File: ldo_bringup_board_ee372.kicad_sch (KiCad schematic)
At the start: 69 parts, among them J1 VIN, J10 MD_SW_EN, J2 GND, J3 IBIAS, J4 VOUT, J5 VIN_SMA, J6 VOUT_SMA, J7 GND, J8 5V, Q1 FDV305N, Q2 FDV305N, Q3 FDV305N, Q4 FDV305N, Q5 FDV305N, SW1 SW_SPDT, U1 LDO_DualMode_BGR_EE372

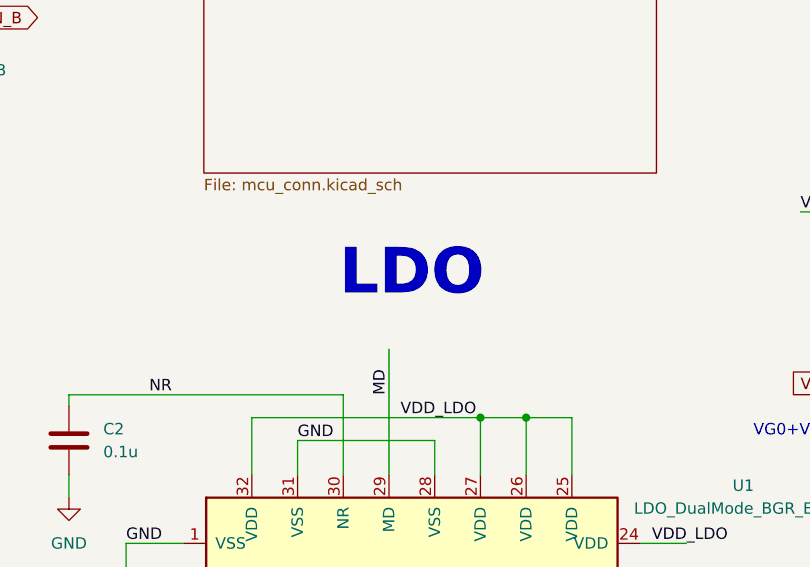
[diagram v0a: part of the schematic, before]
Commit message: Rearrange the MCU sheet and add section titles
Symbols, wires and labels on the MCU sheet moved, and three text notes were
added (MCU, ISENSE AMPS, CONNECTORS). One text position moved on the top
sheet. A netlist export shows the same 105 parts and 79 nets as c5a823f,
with every pin on the same net.
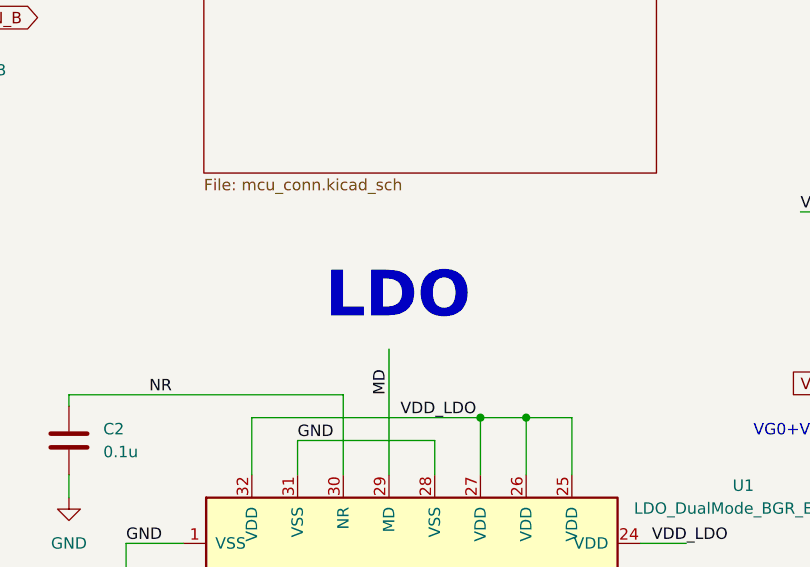
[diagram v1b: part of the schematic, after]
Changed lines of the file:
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@@
 	(text "LDO\n"
 		(exclude_from_sim no)
-		(at 123.19 103.378 0)
+		(at 121.666 105.918 0)
 		(effects
 			(font

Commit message: added buffer
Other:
- added sheet Buffer (buffer.kicad_sch)
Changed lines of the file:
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@@
 	)
 	(sheet
-		(at 159.766 32.512)
+		(at 154.686 14.732)
 		(size 49.784 35.56)
 		(exclude_from_sim no)
@@
 		)
 		(property "Sheetname" "Temperature_Sens"
-			(at 159.766 31.8004 0)
+			(at 154.686 14.0204 0)
 			(show_name no)
 			(do_not_autoplace no)
@@
 		)
 		(property "Sheetfile" "tmp_sense.kicad_sch"
-			(at 159.766 68.6566 0)
+			(at 154.686 50.8766 0)
 			(show_name no)
 			(do_not_autoplace no)
@@
 				)
 			)
+		)
+	)
+	(sheet
+		(at 161.29 58.42)
+		(size 41.91 26.67)
+		(exclude_from_sim no)
+		(in_bom yes)
+		(on_board yes)
+		(dnp no)
+		(fields_autoplaced yes)
+		(stroke
+			(width 0.1524)
+			(type solid)
+		)
+		(fill
+			(color 0 0 0 0)
+		)
+		(property "Sheetname" "Buffer"
+			(at 161.29 57.7084 0)
+			(show_name no)
+			(do_not_autoplace no)
+			(effects
+				(font
+					(size 1.27 1.27)
+				)
+				(justify left bottom)
+			)
+		)
+		(property "Sheetfile" "buffer.kicad_sch"
+			(at 161.29 85.6746 0)
+			(show_name no)
+			(do_not_autoplace no)
+			(effects
+				(font
+					(size 1.27 1.27)
+				)
+				(justify left top)
+			)
+		)
+		(instances
+			(project "ldo_bringup_board_ee372"
+				(path "/d41ff68c-d87d-4b82-b500-4ee675d17cf6"
+					(page "4")
+				)
+			)

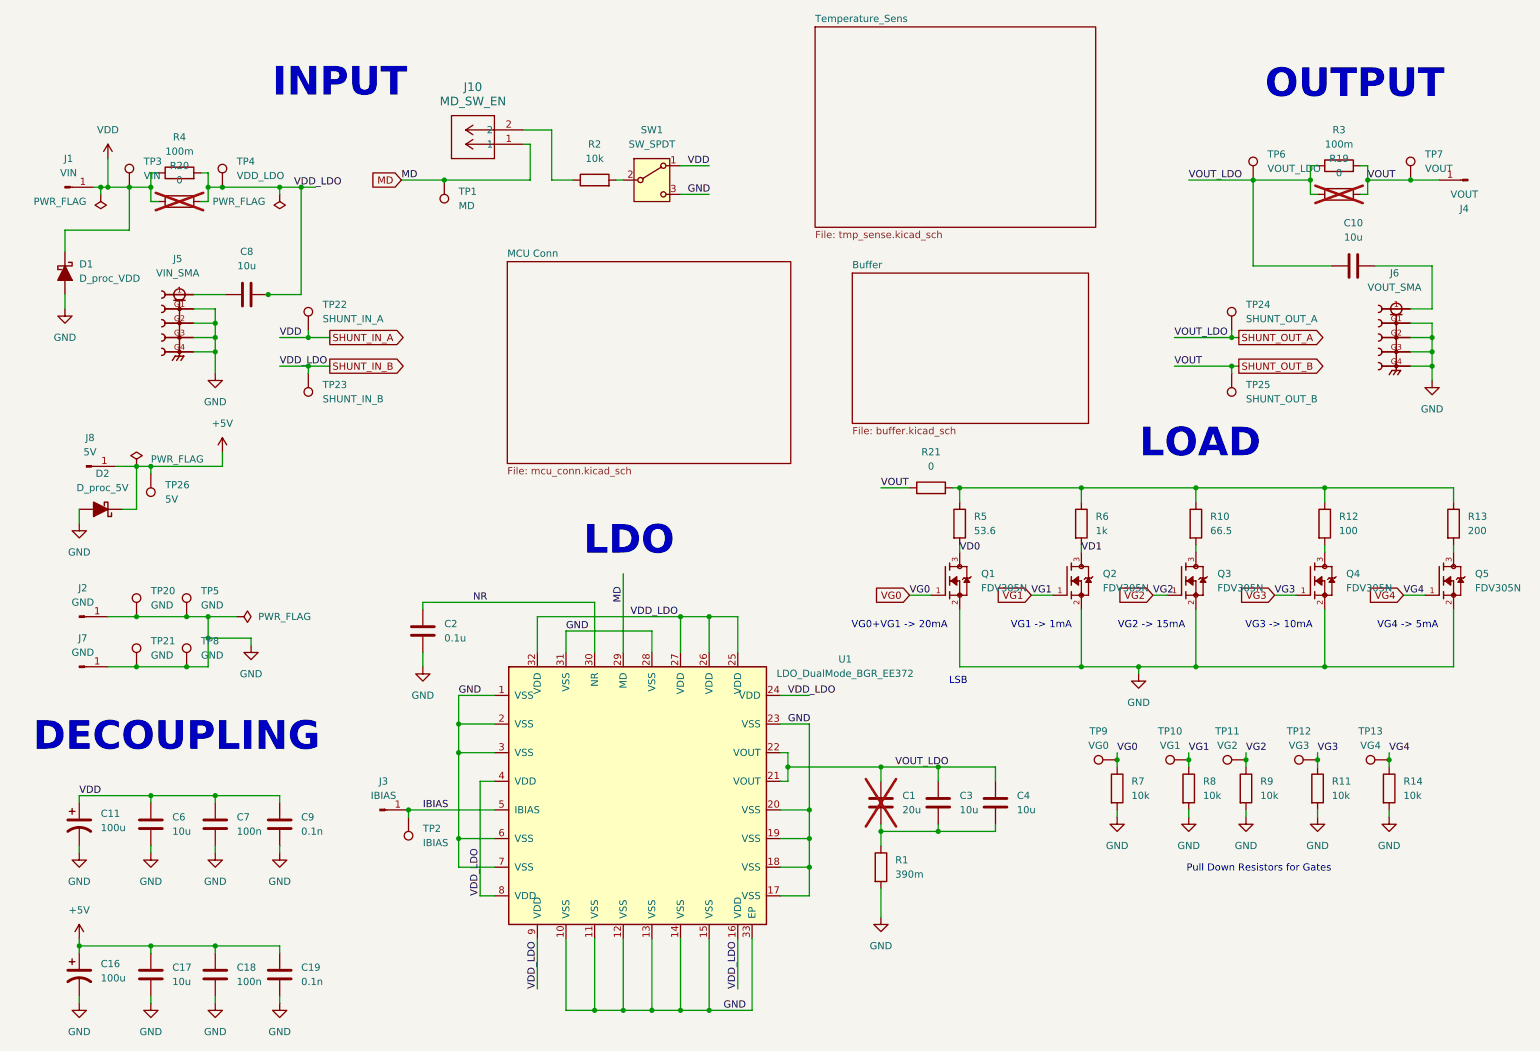
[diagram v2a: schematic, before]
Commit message: Add input filters to both current-sense amplifiers and rework the buffer power
- R29 to R32, in series with the INA190 inputs, change from 0 ohm to 100 ohm,
  and C24 and C25 (100n) go across each amplifier's IN+ and IN-. With the
  100 ohm resistors that is an 8 kHz differential filter on each.
- Buffer sheet. JP4 BUF_EN (2-pin header) replaces J14 between +5V and the
  BUF634A's V+. C23 becomes the 10u 1206 KEMET part, now from V+ to GND. The
  buffer's labels are global now, and R16 joins the buffer output to the VDD
  side of R4 (SHUNT_IN_A).
- One stub wire and its junction removed on the top sheet.

The netlist goes from 113 parts and 85 nets to 115 parts and 84 nets. ERC
shows 1 error, U5's V+ not driven behind JP4, left for the buffer rework along
with V- on GND and five parts that point at the demo board's libraries.
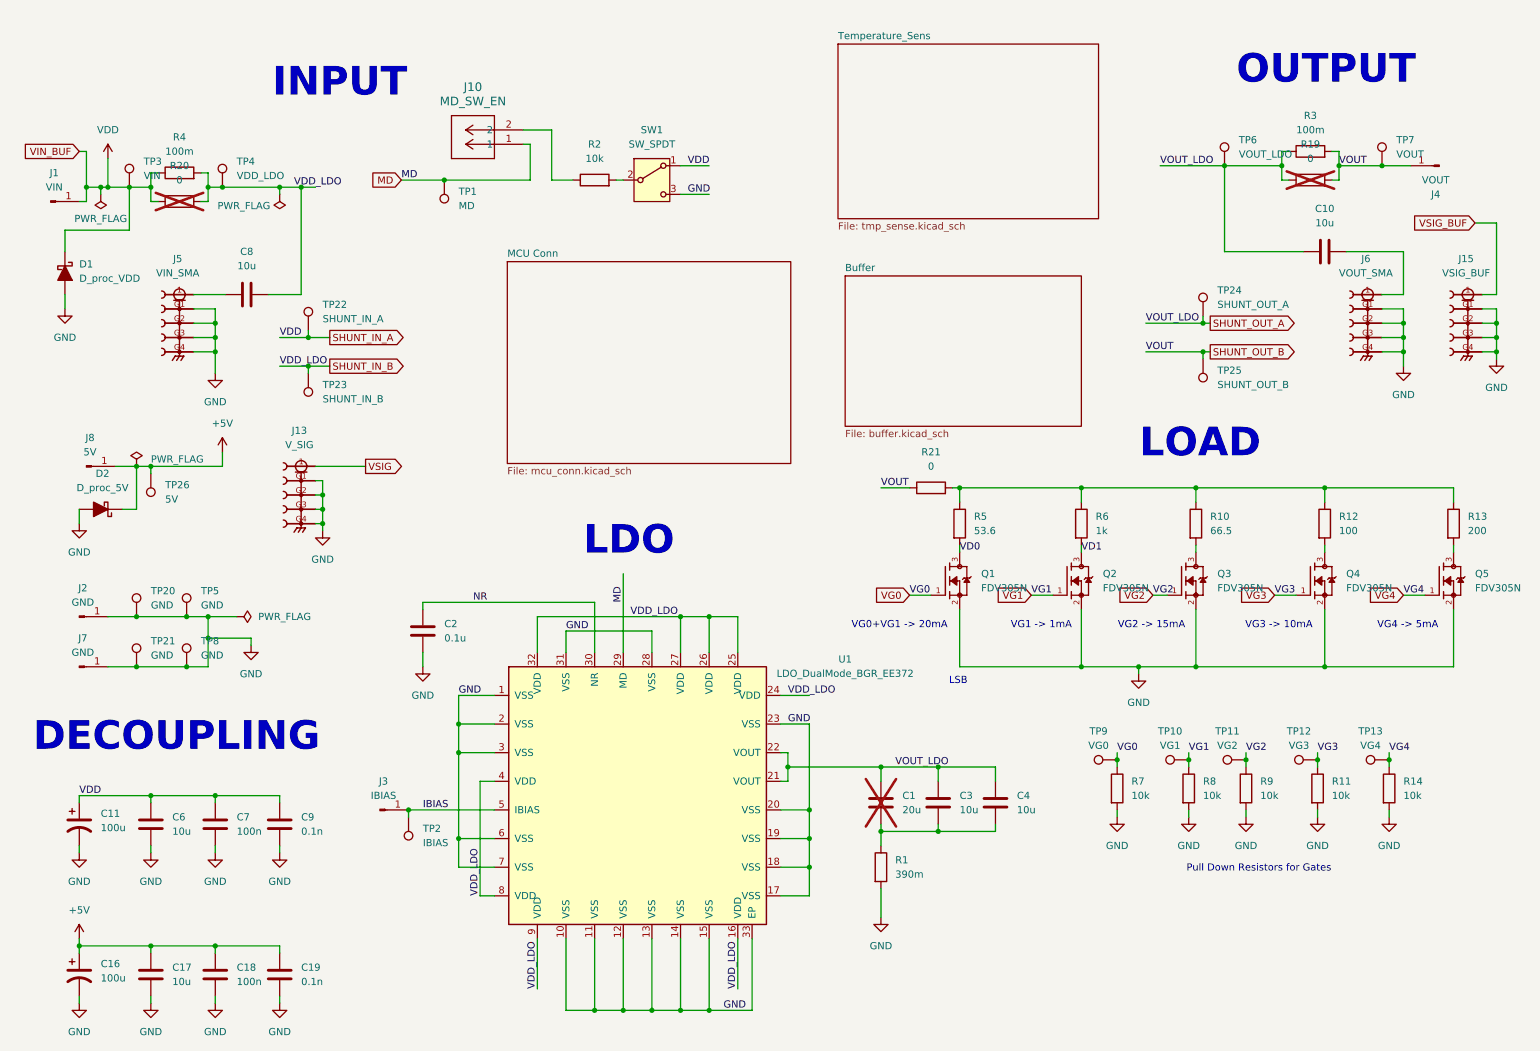
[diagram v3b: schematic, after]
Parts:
- added J13: V_SIG, TPS7A7001_Evaluation_Board_footprint_lib:SAMTEC_SMA-J-P-H-ST-TH1, symbol SMA-J-P-H-ST-TH1:SMA-J-P-H-ST-TH1
- added J15: VSIG_BUF, SMA_J_P_H_ST_TH1:SAMTEC_SMA-J-P-H-ST-TH1, symbol SMA-J-P-H-ST-TH1:SMA-J-P-H-ST-TH1
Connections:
- net GND: now also J13.G1, J13.G2, J13.G3, J13.G4, J15.G1, J15.G2, J15.G3, J15.G4
- new net VSIG: J13.1
- new net VSIG_BUF: J15.1
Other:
- moved on the sheet: C10, J1, J4, J6, R19, R3, TP24, TP25, TP6, TP7
